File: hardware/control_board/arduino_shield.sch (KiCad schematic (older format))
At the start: 7 parts, among them P1 Digital, P2 Power, P3 Analog, P4 Analog, P5 PWM, P6 PWM, P7 Communication

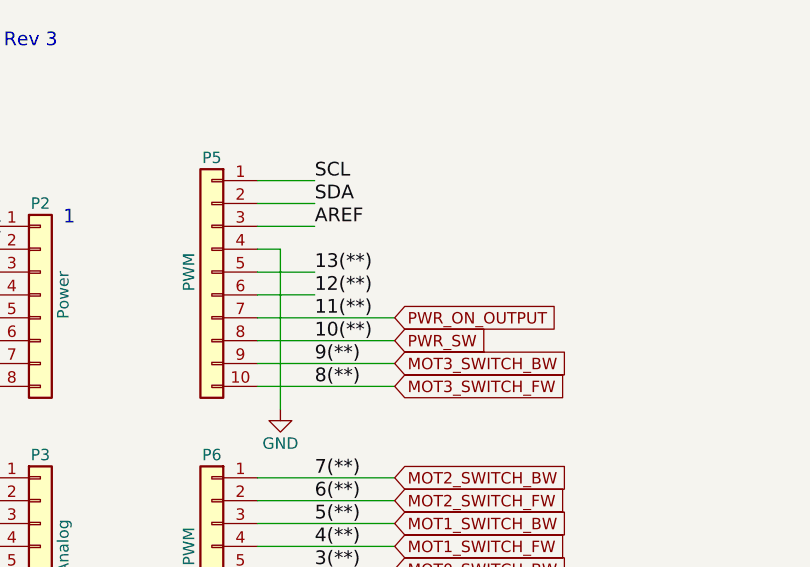
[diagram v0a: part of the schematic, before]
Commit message: update ui control pins
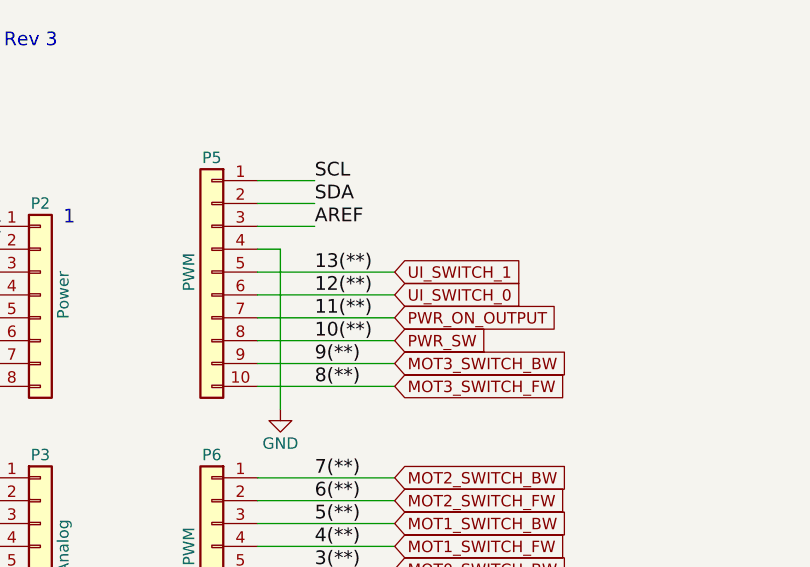
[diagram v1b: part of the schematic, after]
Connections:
- net 12(**) renamed UI_SWITCH_0
- net 13(**) renamed UI_SWITCH_1
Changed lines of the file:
@@
 Wire Wire Line
 	7900 2250 7900 2900
-Wire Wire Line
-	3800 2900 4050 2900
-Wire Wire Line
-	3800 2800 4050 2800
 Text GLabel 7900 3800 3    40   Input ~ 0
 ~MOT3_EN
@@
 Wire Wire Line
 	3800 4200 4400 4200
+Text GLabel 4400 2900 2    50   Input ~ 0
+UI_SWITCH_0
+Text GLabel 4400 2800 2    50   Input ~ 0
+UI_SWITCH_1
+Wire Wire Line
+	3800 2800 4400 2800
+Wire Wire Line
+	3800 2900 4400 2900
 $EndSCHEMATC

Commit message: add misc connectors
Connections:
- net 46 renamed MISC_0
- net 47 renamed MISC_1
- net 48 renamed MISC_2
- net 49 renamed MISC_3
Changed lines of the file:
@@
 	3800 5350 4050 5350
 Wire Wire Line
-	7800 2900 7800 2700
-Wire Wire Line
-	7700 2900 7700 2700
-Wire Wire Line
 	7600 2900 7600 2700
 Wire Wire Line
 	7500 2900 7500 2700
-Wire Wire Line
-	7800 3400 7800 3700
-Wire Wire Line
-	7700 3400 7700 3700
 Wire Wire Line
 	7600 3400 7600 3800
@@
 Wire Wire Line
 	3800 2900 4400 2900
+Text GLabel 7800 2250 1    50   Input ~ 0
+MISC_0
+Text GLabel 7700 2250 1    50   Input ~ 0
+MISC_2
+Text GLabel 7800 3800 3    50   Input ~ 0
+MISC_1
+Text GLabel 7700 3800 3    50   Input ~ 0
+MISC_3
+Wire Wire Line
+	7700 3400 7700 3800
+Wire Wire Line
+	7800 3400 7800 3800
+Wire Wire Line
+	7800 2250 7800 2900
+Wire Wire Line
+	7700 2250 7700 2900
 $EndSCHEMATC

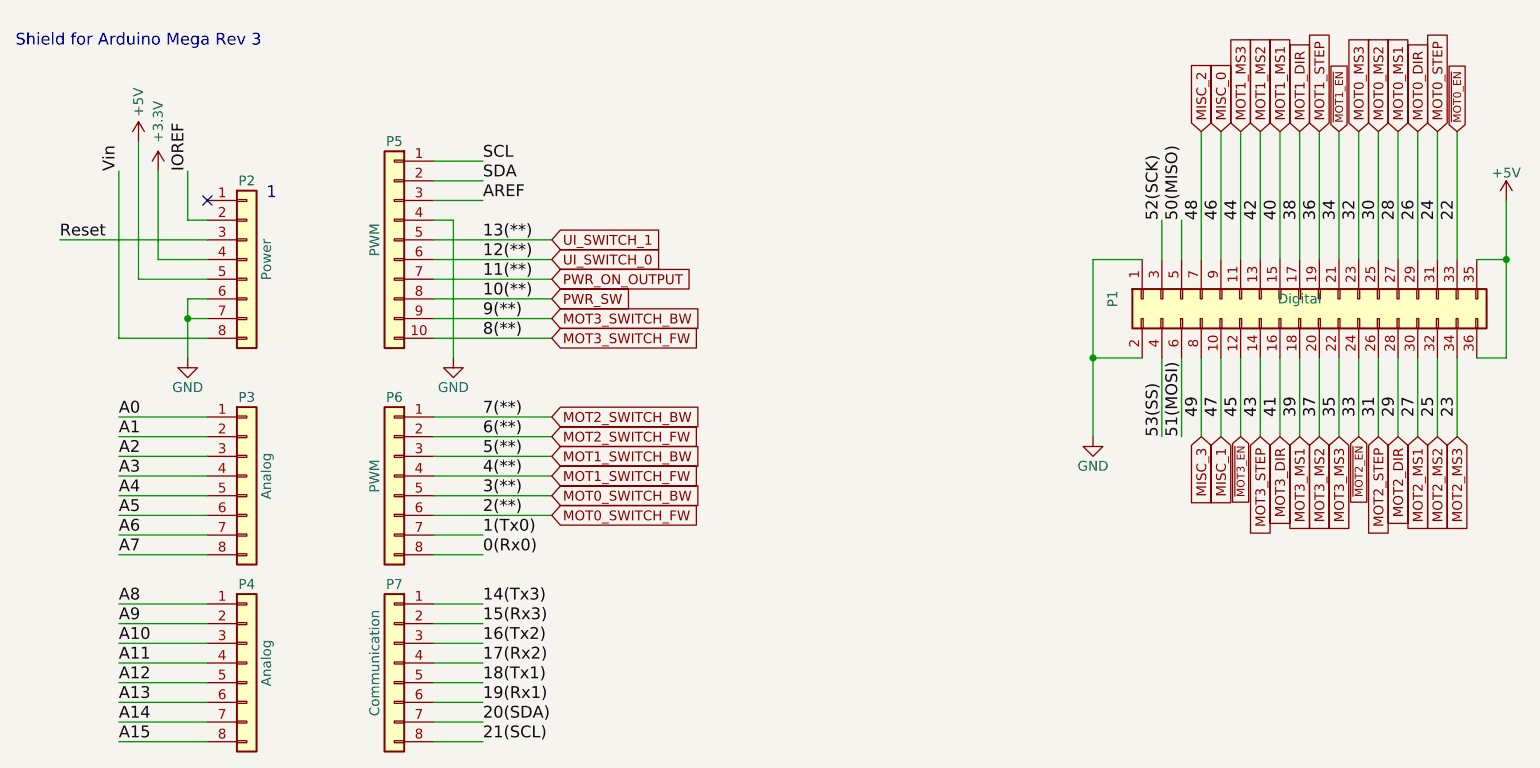
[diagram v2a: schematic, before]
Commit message: finish layout, add fusing
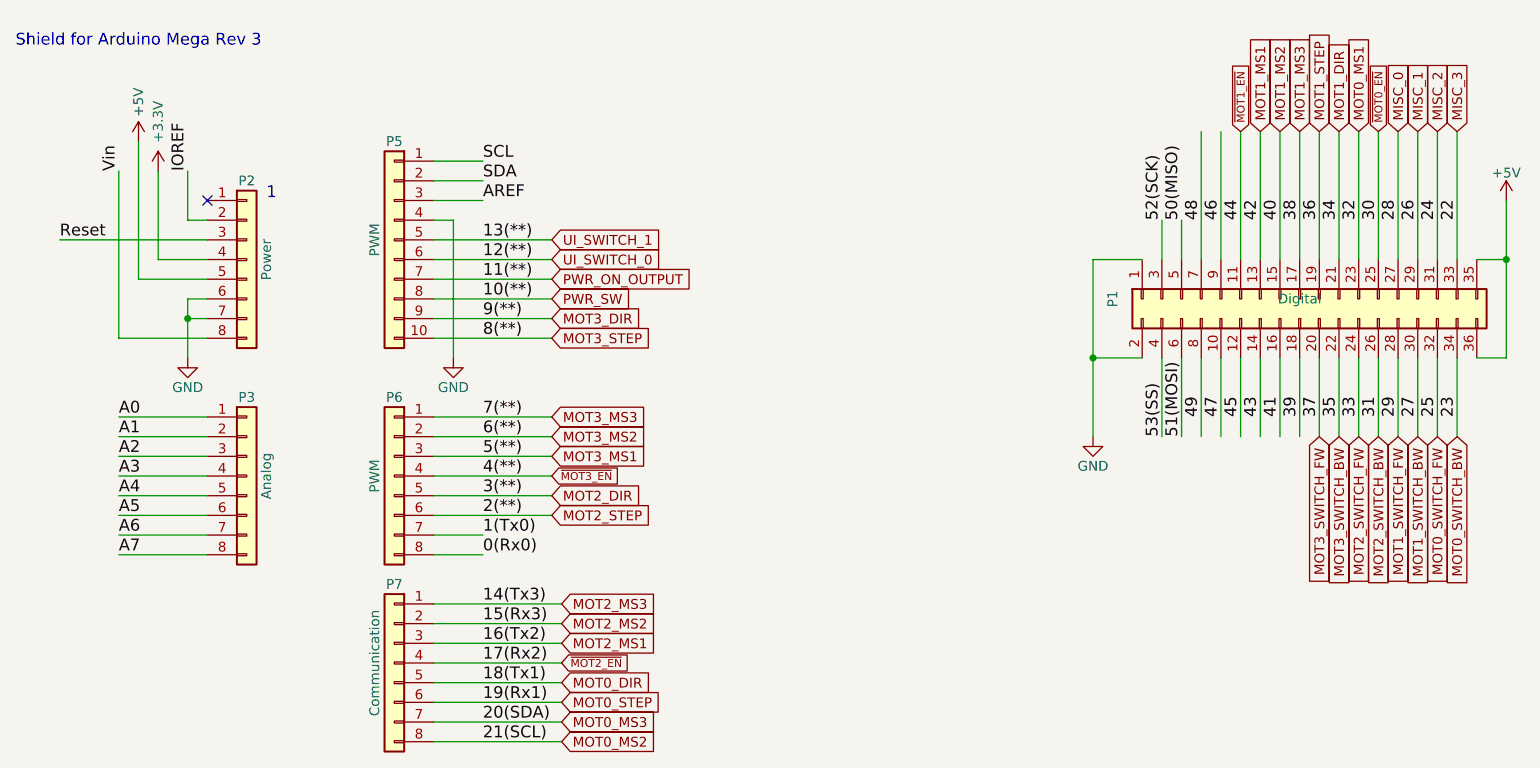
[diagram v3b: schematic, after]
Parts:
- removed P4: Analog, Socket_Arduino_Mega:Socket_Strip_Arduino_1x08, symbol Connector_Generic:Conn_01x08
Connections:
- net labels removed: A10, A11, A12, A13, A14, A15, A8, A9
- wire segments 96 -> 88
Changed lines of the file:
@@
 Text Label 2200 4400 0    60   ~ 0
 A7
-Text Label 2200 4650 0    60   ~ 0
-A8
-Text Label 2200 4750 0    60   ~ 0
-A9
-Text Label 2200 4850 0    60   ~ 0
-A10
-Text Label 2200 4950 0    60   ~ 0
-A11
-Text Label 2200 5050 0    60   ~ 0
-A12
-Text Label 2200 5150 0    60   ~ 0
-A13
-Text Label 2200 5250 0    60   ~ 0
-A14
-Text Label 2200 5350 0    60   ~ 0
-A15
 Text Label 9000 2700 1    60   ~ 0
 22
@@
 $Comp
 L Connector_Generic:Conn_01x08 P?
-U 1 1 618913F0
-P 2850 4950
-AR Path="/618913F0" Ref="P?"  Part="1"
-AR Path="/6187679E/618913F0" Ref="P4"  Part="1"
-F 0 "P4" H 2850 5350 50  0000 C CNN
-F 1 "Analog" V 2950 4950 50  0000 C CNN
-F 2 "Socket_Arduino_Mega:Socket_Strip_Arduino_1x08" H 2850 4950 50  0001 C CNN
-F 3 "" H 2850 4950 50  0000 C CNN
-	1    2850 4950
-	1    0    0    -1
-$EndComp
-$Comp
-L Connector_Generic:Conn_01x08 P?
 U 1 1 618913F6
 P 3600 4950
@@
 	3800 4400 4050 4400
 Wire Wire Line
-	2650 4650 2200 4650
-Wire Wire Line
-	2200 4750 2650 4750
-Wire Wire Line
-	2650 4850 2200 4850
-Wire Wire Line
-	2200 4950 2650 4950
-Wire Wire Line
-	2650 5050 2200 5050
-Wire Wire Line
-	2200 5150 2650 5150
-Wire Wire Line
-	2650 5250 2200 5250
-Wire Wire Line
-	2200 5350 2650 5350
-Wire Wire Line
-	4050 4650 3800 4650
-Wire Wire Line
-	3800 4750 4050 4750
-Wire Wire Line
-	4050 4850 3800 4850
-Wire Wire Line
-	3800 4950 4050 4950
-Wire Wire Line
-	4050 5050 3800 5050
-Wire Wire Line
-	3800 5150 4050 5150
-Wire Wire Line
-	4050 5250 3800 5250
-Wire Wire Line
-	3800 5350 4050 5350
-Wire Wire Line
 	7600 2900 7600 2700
 Wire Wire Line
@@
 Wire Wire Line
 	7150 3400 7150 3800
-Text GLabel 9000 2250 1    40   Input ~ 0
+Text GLabel 8600 2250 1    40   Input ~ 0
 ~MOT0_EN
-Text GLabel 8900 2250 1    50   Input ~ 0
+Text GLabel 4450 5150 2    50   Input ~ 0
 MOT0_STEP
-Text GLabel 8800 2250 1    50   Input ~ 0
+Text GLabel 4450 5050 2    50   Input ~ 0
 MOT0_DIR
-Text GLabel 8700 2250 1    50   Input ~ 0
+Text GLabel 8500 2250 1    50   Input ~ 0
 MOT0_MS1
-Text GLabel 8600 2250 1    50   Input ~ 0
+Text GLabel 4450 5350 2    50   Input ~ 0
 MOT0_MS2
-Text GLabel 8500 2250 1    50   Input ~ 0
+Text GLabel 4450 5250 2    50   Input ~ 0
 MOT0_MS3
-Text GLabel 8400 2250 1    40   Input ~ 0
+Text GLabel 7900 2250 1    40   Input ~ 0
 ~MOT1_EN
 Text GLabel 8300 2250 1    50   Input ~ 0
 MOT1_STEP
+Text GLabel 8400 2250 1    50   Input ~ 0
+MOT1_DIR
+Text GLabel 8000 2250 1    50   Input ~ 0
+MOT1_MS1
+Text GLabel 8100 2250 1    50   Input ~ 0
+MOT1_MS2
 Text GLabel 8200 2250 1    50   Input ~ 0
-MOT1_DIR
-Text GLabel 8100 2250 1    50   Input ~ 0
-MOT1_MS1
-Text GLabel 8000 2250 1    50   Input ~ 0
-MOT1_MS2
-Text GLabel 7900 2250 1    50   Input ~ 0
 MOT1_MS3
-Text GLabel 8500 3800 3    40   Input ~ 0
+Text GLabel 4450 4950 2    40   Input ~ 0
 ~MOT2_EN
+Text GLabel 4400 4200 2    50   Input ~ 0
+MOT2_STEP
+Text GLabel 4400 4100 2    50   Input ~ 0
+MOT2_DIR
+Text GLabel 4450 4850 2    50   Input ~ 0
+MOT2_MS1
+Text GLabel 4450 4750 2    50   Input ~ 0
+MOT2_MS2
+Text GLabel 4450 4650 2    50   Input ~ 0
+MOT2_MS3
+Wire Wire Line
+	9000 2250 9000 2900
+Wire Wire Line
+	8900 2250 8900 2900
+Wire Wire Line
+	8800 2250 8800 2900
+Wire Wire Line
+	8700 2250 8700 2900
+Wire Wire Line
+	8600 2250 8600 2900
+Wire Wire Line
+	8500 2250 8500 2900
+Wire Wire Line
+	8400 2250 8400 2900
+Wire Wire Line
+	8300 2250 8300 2900
+Wire Wire Line
+	8200 2250 8200 2900
+Wire Wire Line
+	8100 2250 8100 2900
+Wire Wire Line
+	8000 2250 8000 2900
+Wire Wire Line
+	7900 2250 7900 2900
+Text GLabel 4400 4000 2    40   Input ~ 0
+~MOT3_EN
+Text GLabel 4400 3900 2    50   Input ~ 0
+MOT3_MS1
+Text GLabel 4400 3800 2    50   Input ~ 0
+MOT3_MS2
+Text GLabel 4400 3700 2    50   Input ~ 0
+MOT3_MS3
+Wire Wire Line
+	8100 3400 8100 3800
+Wire Wire Line
+	8000 3400 8000 3800
+Wire Wire Line
+	7900 3400 7900 3800
+Wire Wire Line
+	8200 3400 8200 3800
+Wire Wire Line
+	8300 3400 8300 3800
+Wire Wire Line
+	8400 3400 8400 3800
+Wire Wire Line
+	8500 3400 8500 3800
+Wire Wire Line
+	8600 3400 8600 3800
+Wire Wire Line
+	8700 3400 8700 3800
+Wire Wire Line
+	8800 3400 8800 3800
+Wire Wire Line
+	8900 3400 8900 3800
+Wire Wire Line
+	9000 3400 9000 3800
+Text GLabel 8900 3800 3    50   Input ~ 0
+MOT0_SWITCH_FW
+Text GLabel 8700 3800 3    50   Input ~ 0
+MOT1_SWITCH_FW
+Text GLabel 8500 3800 3    50   Input ~ 0
+MOT2_SWITCH_FW
+Text GLabel 8300 3800 3    50   Input ~ 0
+MOT3_SWITCH_FW
+Text GLabel 9000 3800 3    50   Input ~ 0
+MOT0_SWITCH_BW
+Text GLabel 8800 3800 3    50   Input ~ 0
+MOT1_SWITCH_BW
 Text GLabel 8600 3800 3    50   Input ~ 0
-MOT2_STEP
-Text GLabel 8700 3800 3    50   Input ~ 0
-MOT2_DIR
-Text GLabel 8800 3800 3    50   Input ~ 0
-MOT2_MS1
-Text GLabel 8900 3800 3    50   Input ~ 0
-MOT2_MS2
-Text GLabel 9000 3800 3    50   Input ~ 0
-MOT2_MS3
-Wire Wire Line
-	9000 2250 9000 2900
-Wire Wire Line
-	8900 2250 8900 2900
-Wire Wire Line
-	8800 2250 8800 2900
-Wire Wire Line
-	8700 2250 8700 2900
-Wire Wire Line
-	8600 2250 8600 2900
-Wire Wire Line
-	8500 2250 8500 2900
-Wire Wire Line
-	8400 2250 8400 2900
-Wire Wire Line
-	8300 2250 8300 2900
-Wire Wire Line
-	8200 2250 8200 2900
-Wire Wire Line
-	8100 2250 8100 2900
-Wire Wire Line
-	8000 2250 8000 2900
-Wire Wire Line
-	7900 2250 7900 2900
-Text GLabel 7900 3800 3    40   Input ~ 0
-~MOT3_EN
-Text GLabel 8000 3800 3    50   Input ~ 0
-MOT3_STEP
-Text GLabel 8100 3800 3    50   Input ~ 0
-MOT3_DIR
-Text GLabel 8200 3800 3    50   Input ~ 0
-MOT3_MS1
-Text GLabel 8300 3800 3    50   Input ~ 0
-MOT3_MS2
+MOT2_SWITCH_BW
 Text GLabel 8400 3800 3    50   Input ~ 0
-MOT3_MS3
-Wire Wire Line
-	8100 3400 8100 3800
-Wire Wire Line
-	8000 3400 8000 3800
-Wire Wire Line
-	7900 3400 7900 3800
-Wire Wire Line
-	8200 3400 8200 3800
-Wire Wire Line
-	8300 3400 8300 3800
-Wire Wire Line
-	8400 3400 8400 3800
-Wire Wire Line
-	8500 3400 8500 3800
-Wire Wire Line
-	8600 3400 8600 3800
-Wire Wire Line
-	8700 3400 8700 3800
-Wire Wire Line
-	8800 3400 8800 3800
-Wire Wire Line
-	8900 3400 8900 3800
-Wire Wire Line
-	9000 3400 9000 3800
-Text GLabel 4400 4200 2    50   Input ~ 0
-MOT0_SWITCH_FW
-Text GLabel 4400 4000 2    50   Input ~ 0
-MOT1_SWITCH_FW
-Text GLabel 4400 3800 2    50   Input ~ 0
-MOT2_SWITCH_FW
-Text GLabel 4400 3300 2    50   Input ~ 0
-MOT3_SWITCH_FW
-Text GLabel 4400 4100 2    50   Input ~ 0
-MOT0_SWITCH_BW
-Text GLabel 4400 3900 2    50   Input ~ 0
-MOT1_SWITCH_BW
-Text GLabel 4400 3700 2    50   Input ~ 0
-MOT2_SWITCH_BW
-Text GLabel 4400 3200 2    50   Input ~ 0
 MOT3_SWITCH_BW
 Wire Wire Line
@@
 Wire Wire Line
 	3800 2900 4400 2900
-Text GLabel 7800 2250 1    50   Input ~ 0
+Wire Wire Line
+	7700 3400 7700 3800
+Wire Wire Line
+	7800 3400 7800 3800
+Wire Wire Line
+	7800 2250 7800 2900
+Wire Wire Line
+	7700 2250 7700 2900
+Text GLabel 8800 2250 1    50   Input ~ 0
+MISC_1
+Text GLabel 9000 2250 1    50   Input ~ 0
+MISC_3
+Text GLabel 8700 2250 1    50   Input ~ 0
 MISC_0
-Text GLabel 7700 2250 1    50   Input ~ 0
+Text GLabel 8900 2250 1    50   Input ~ 0
 MISC_2
-Text GLabel 7800 3800 3    50   Input ~ 0
-MISC_1
-Text GLabel 7700 3800 3    50   Input ~ 0
-MISC_3
-Wire Wire Line
-	7700 3400 7700 3800
-Wire Wire Line
-	7800 3400 7800 3800
-Wire Wire Line
-	7800 2250 7800 2900
-Wire Wire Line
-	7700 2250 7700 2900
+Wire Wire Line
+	3800 4750 4450 4750
+Wire Wire Line
+	3800 4850 4450 4850
+Wire Wire Line
+	3800 4950 4450 4950
+Wire Wire Line
+	3800 4650 4450 4650
+Wire Wire Line
+	3800 5050 4450 5050
+Wire Wire Line
+	3800 5150 4450 5150
+Text GLabel 4400 3200 2    50   Input ~ 0
+MOT3_DIR
+Text GLabel 4400 3300 2    50   Input ~ 0
+MOT3_STEP
+Wire Wire Line
+	3800 5250 4450 5250
+Wire Wire Line
+	3800 5350 4450 5350
 $EndSCHEMATC
